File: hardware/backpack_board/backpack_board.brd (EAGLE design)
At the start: 35.6 x 49.5 mm, 21 parts, among them Q1 MOSFET-NCHANNEL2N7000

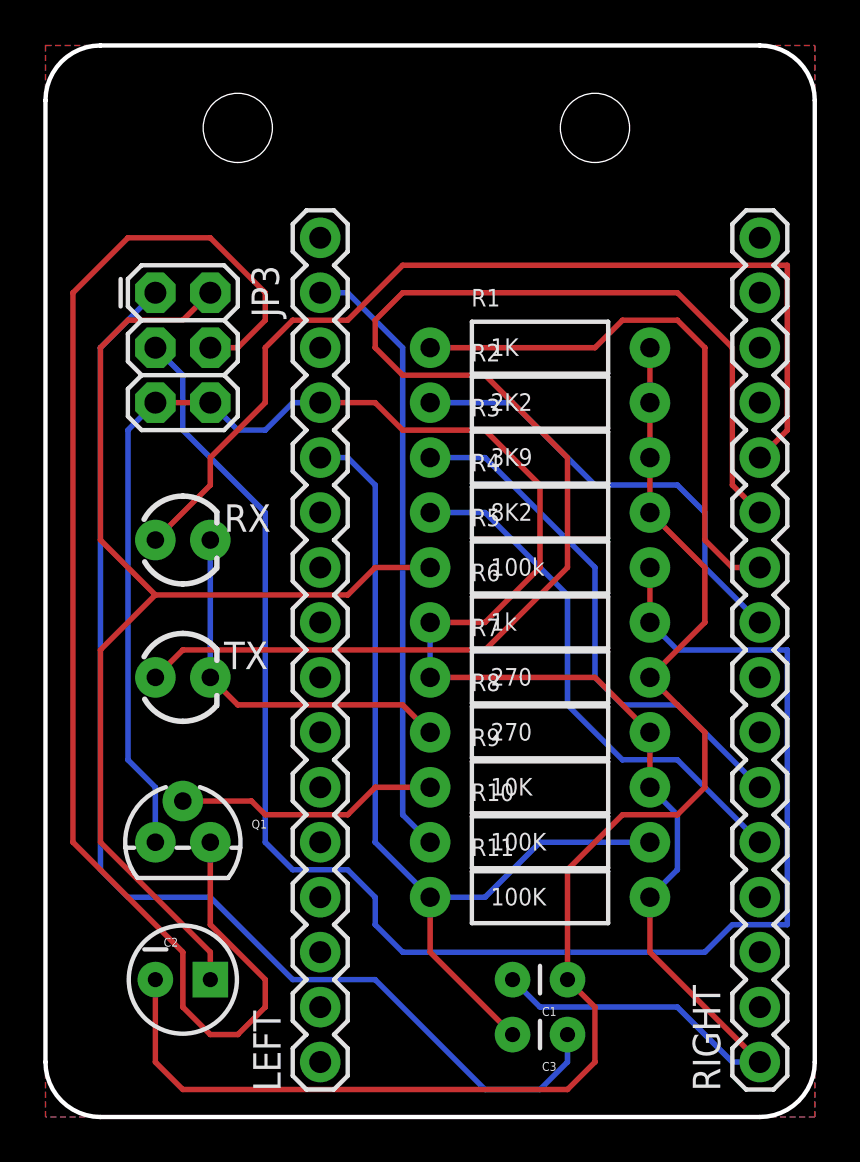
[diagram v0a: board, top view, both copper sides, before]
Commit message: add silkscreen and drill holes to design
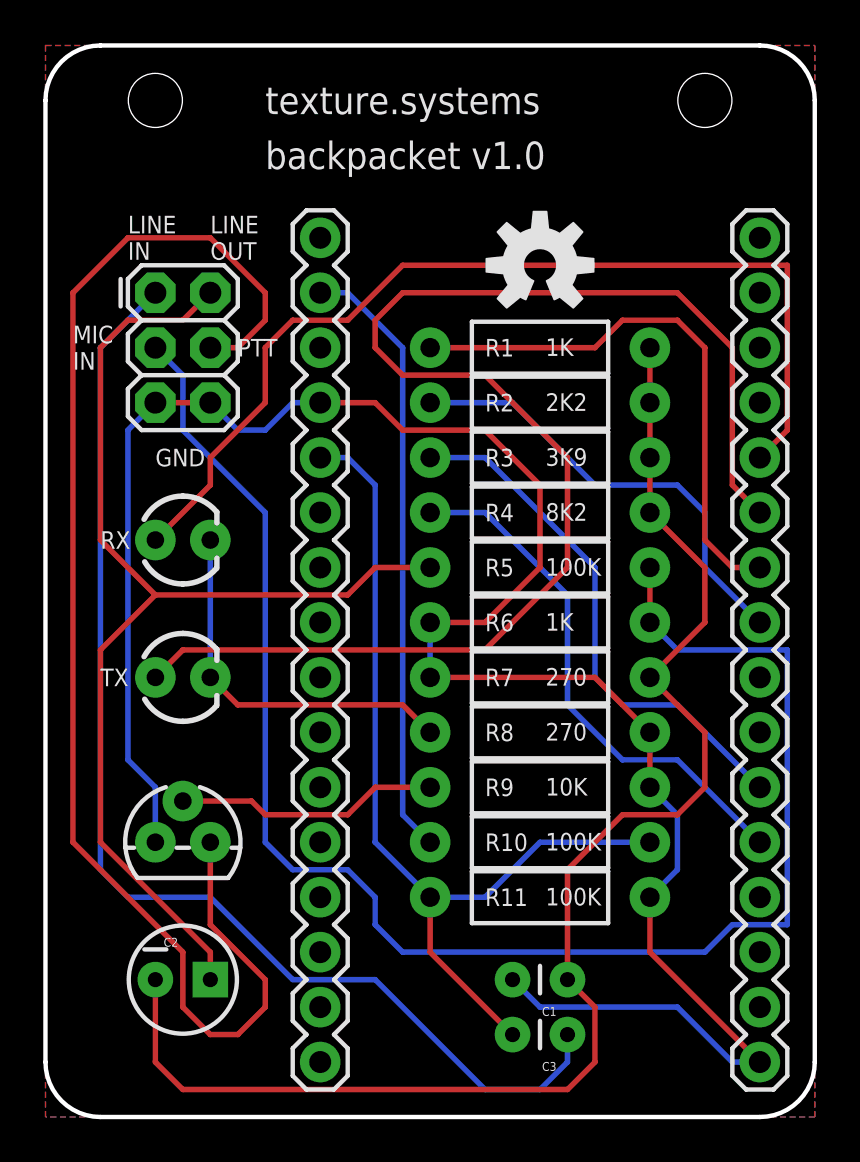
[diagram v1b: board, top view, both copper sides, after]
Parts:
- added LOGO1: OSHW-LOGOM, SparkFun-Aesthetics:OSHW-LOGO-M
- R5: value 100k -> 100K
- R6: value 1k -> 1K
- RADIO: value FEMALE 2x3 -> (none)
- renumbered JP3 to RADIO
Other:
- board text added: "GND"
- board text added: "LINE IN"
- board text added: "LINE OUT"
- board text added: "MIC IN"
- board text added: "PTT"
- board text added: "R1"
- board text added: "R10"
- board text added: "R11"
- board text added: "R2"
- board text added: "R3"
- board text added: "R4"
- board text added: "R5"
- board text added: "R6"
- board text added: "R7"
- board text added: "R8"
- board text added: "R9"
- board text added: "RX"
- board text added: "TX"
- board text added: "backpacket v1.0"
- board text added: "texture.systems"

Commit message: add power switch
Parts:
- added POWER: (no value), SparkFun-Connectors:1X02
- added SWITCH: (no value), SparkFun-Electromechanical:SWITCH-SPDT
- moved C2 2.84 mm to (11.4, 34.3)
- moved Q1 1.27 mm to (11.4, 43.2), turned to 270 degrees
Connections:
- new net N$2: POWER.2, SWITCH.2
- new net SWITCH: POWER.1, SWITCH.3
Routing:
- net N$2: track 0.00 -> 35.3 mm
- net SWITCH: track 0.00 -> 29.2 mm
- net PTT_V+: track 64.0 -> 69.0 mm
- net GND: track 96.9 -> 92.3 mm
- net N$1: track 66.0 -> 62.2 mm
- net LINE_LEVEL_OUT: track 52.8 -> 55.8 mm
- net D3: track 12.2 -> 9.31 mm
- net LINE_LEVEL_IN: track 55.3 -> 52.8 mm
